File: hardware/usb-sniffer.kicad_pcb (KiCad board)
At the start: 2 copper layers, 58.2 x 38.1 mm, 87 parts, among them IC1 LCMXO2-2000HC-5TG100, IC10 DSC6101CI2A-024.0000, IC2 MIC5504-3.3v, IC3 MAX9032AKA+T, IC4 USB3343, IC5 MAX9032AKA+T, IC6 DSC6101CI2A-026.0000, IC7 MAX9032AKA+T, IC8 24LC128, IC9 CY7C68013A-56PVXC, J1 USB-C, J2 USB-C, J3 USB-A, J4 IN, J5 GND

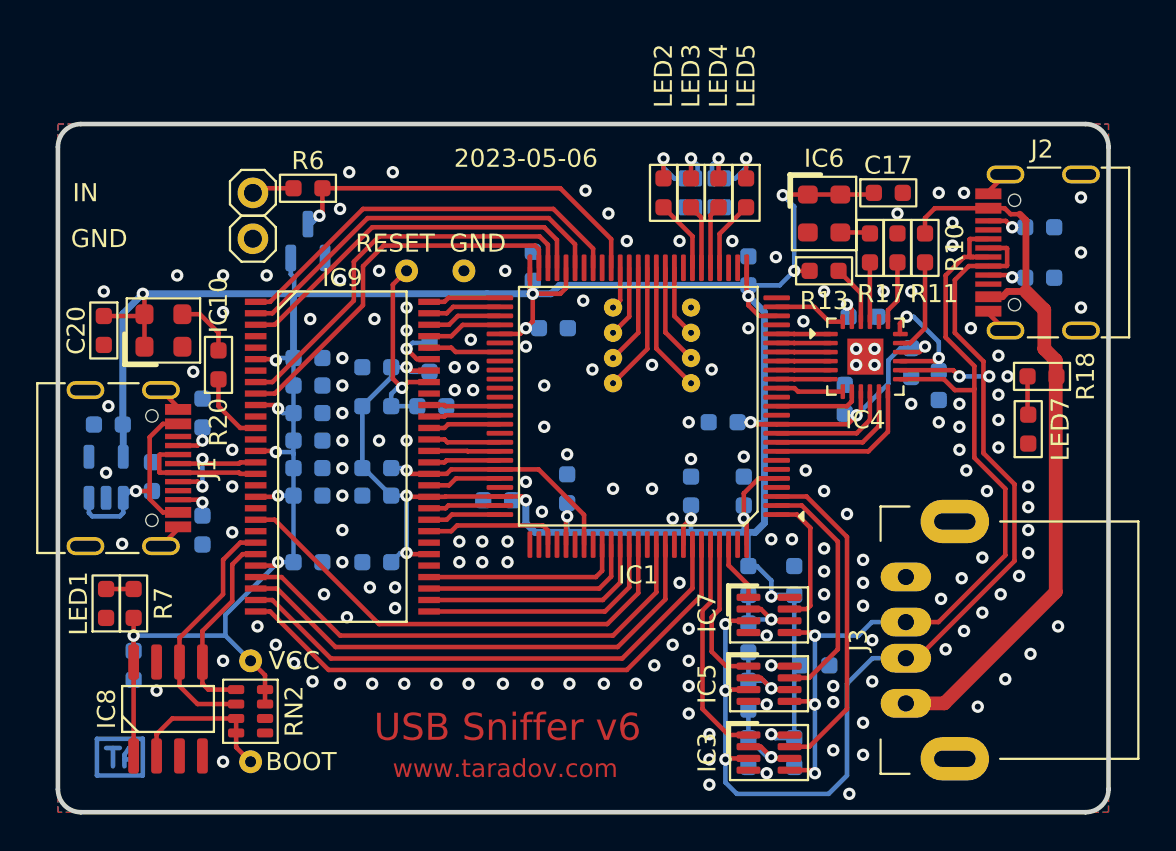
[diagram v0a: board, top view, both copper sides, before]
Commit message: Select parts for JLCPCB assembly
Also, modify USB type-A connector for an SMD part that is widely in
stocked.
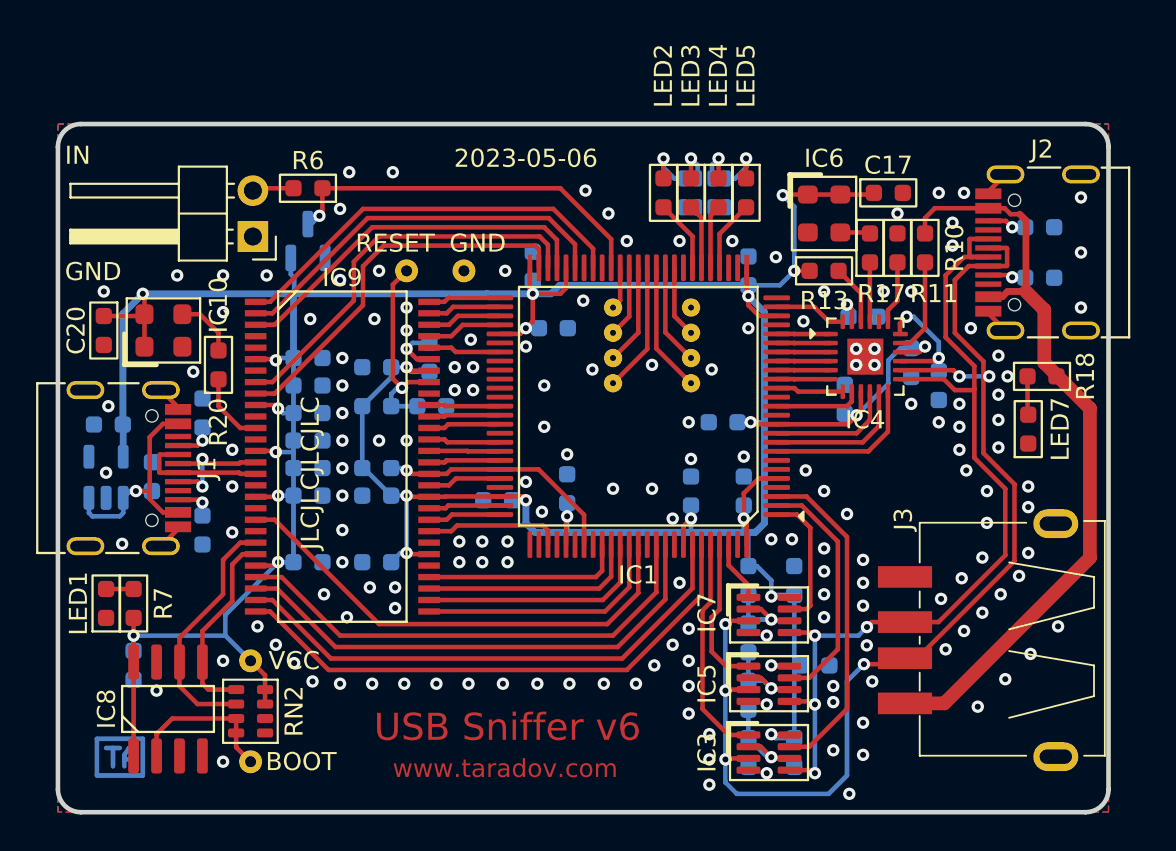
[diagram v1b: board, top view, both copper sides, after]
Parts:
- removed J5: GND, ataradov_conn:Pin-2.54mm
- J3: footprint ataradov_conn:USB-A-Slots -> usb-sniffer:C668591
- J4: footprint ataradov_conn:Pin-2.54mm -> Connector_PinHeader_2.54mm:PinHeader_1x02_P2.54mm_Horizontal
- moved J3 3.96 mm to (74.6, 57.9)
- moved J4 2.42 mm to (31.8, 35.6), turned to 180 degrees
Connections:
- J4 pad 1: Net-(J4-Pad1) -> GND
- R6 pad 1: Net-(J4-Pad1) -> Net-(J4-Pin_2)
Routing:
- net Net-(J4-Pin_2): track 0.00 -> 2.35 mm
- net Net-(J4-Pad1): track 2.35 -> 0.00 mm
- net /T_USB_VBUS: track 41.3 -> 42.8 mm
- net /T_USB_DP: track 50.7 -> 50.6 mm, vias 3 -> 4
- net /T_USB_DM: track 64.5 -> 64.6 mm, vias 5 -> 6
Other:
- board text added: "IN GND"
- board text added: "JLCJLCJLCJLC"
